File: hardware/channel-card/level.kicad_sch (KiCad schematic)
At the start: 59 parts, among them SW201 MUTE (latching), SW202 DUCK (latching), U201 SSI2162, U202 NE5532, U203 NE5532, U204 TL072, U205 TL072, U206 DG413DY

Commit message: Redraw level sheet with real wires
Pilot for readable sheets: schlayout.py places symbols and draws wires
from KiCad pin geometry, level_wired.py lays out the Level sheet by
circuit block, post_wired.py adds junctions, ground nets, no-connects
and readable field placement. level_build.py stays the reference
netlist. SSI2162 symbol pins rearranged for drawing.

Co-Authored-By: Claude Opus 5.5 <noreply@anthropic.com>
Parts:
- U201: SupplierPN (none) -> 41019302
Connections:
- net +15V: now also R206.1; no longer R206.2
- net AGND: now also C222.1, R220.1, R222.1; no longer C222.2, R220.2, R222.2
- net DUCK_CTRL: now also R222.2; no longer R222.1
- net MUTE_CTRL: now also R220.2; no longer R220.1
- net DUCK_LED: no longer names the net of D204.2 (A), R221.2
- net DUCK_LEDK: no longer names the net of D204.1 (K), SW202.4 (A)
- net DUCK_V: no longer names the net of R217.1, U206.2
- net FADW: no longer names the net of RV201.2, U204.3 (+)
- net L_IIN: no longer names the net of R201.2, U201.2 (IIN1)
- net L_IIN: now also R202.2; no longer R202.1
- net L_INV: no longer names the net of R204.2, R205.1, U203.2 (-)
- net L_IOUT: no longer names the net of C223.1, R203.1, U201.4 (IOUT1), U202.2 (-)
- removed net L_RC: C222.1, R202.2
- net L_VIN: no longer names the net of C221.2, R201.1
- net L_VO: no longer names the net of C223.2, R203.2, R204.1, U202.1
- net MODE: no longer names the net of U201.1 (MODE)
- net MODE: now also R206.2; no longer R206.1
- net MUTE_LED: no longer names the net of D203.2 (A), R219.2
- net MUTE_LEDK: no longer names the net of D203.1 (K), SW201.4 (A)
- net R_IIN: no longer names the net of R251.2, R252.1, U201.9 (IIN2)
- net R_INV: no longer names the net of R254.2, R255.1, U203.6 (-)
- net R_IOUT: no longer names the net of C273.1, R253.1, U201.7 (IOUT2), U202.6 (-)
- net R_RC: no longer names the net of C272.1, R252.2
- net R_VIN: no longer names the net of C271.2, R251.1
- net R_VO: no longer names the net of C273.2, R253.2, R254.1, U202.7
- net SD1IN: no longer names the net of R209.2, R210.2, U204.5 (+)
- net SD1K: no longer names the net of D201.2 (A), R211.1, U204.6 (-)
- net SD1O: no longer names the net of D201.1 (K), U204.7
- net SD2IN: no longer names the net of R212.2, R213.2, U205.3 (+)
- net SD2K: no longer names the net of D202.2 (A), R214.1, U205.2 (-)
- net SD2O: no longer names the net of D202.1 (K), U205.1
- net VB: no longer names the net of R207.1, R209.1, R212.1, U204.1, U204.2 (-)
- net VSUM: no longer names the net of C224.1, R207.2, R208.2, R211.2, R214.2, R215.1, R216.2, U205.6 (-)
- new net: C222.2, R202.1

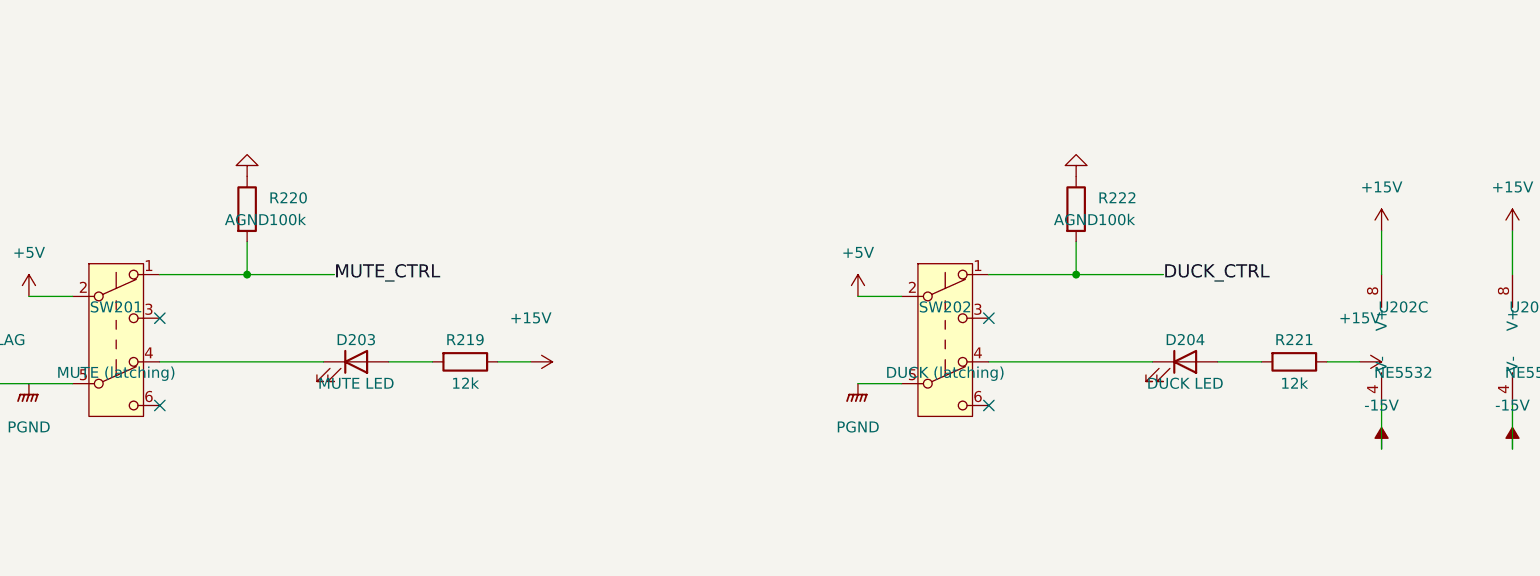
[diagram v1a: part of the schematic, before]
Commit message: Choose GPBS850N latching buttons with printed light caps
Buttons are CW Industries GPBS850N latching DPDT switches (Electrokit)
with 0805 LEDs lighting 3D-printed translucent caps (decision 75).
The datasheet shows pins 2-3 and 5-6 close when pressed, so every
button now uses pin 3 for logic and pin 6 for the LED. Adds the switch
footprint library, rebuild_all.sh, the state-retention requirement for
the momentary-button backlog item, and ten switches to the second
Electrokit order.

Co-Authored-By: Claude Opus 5.5 <noreply@anthropic.com>
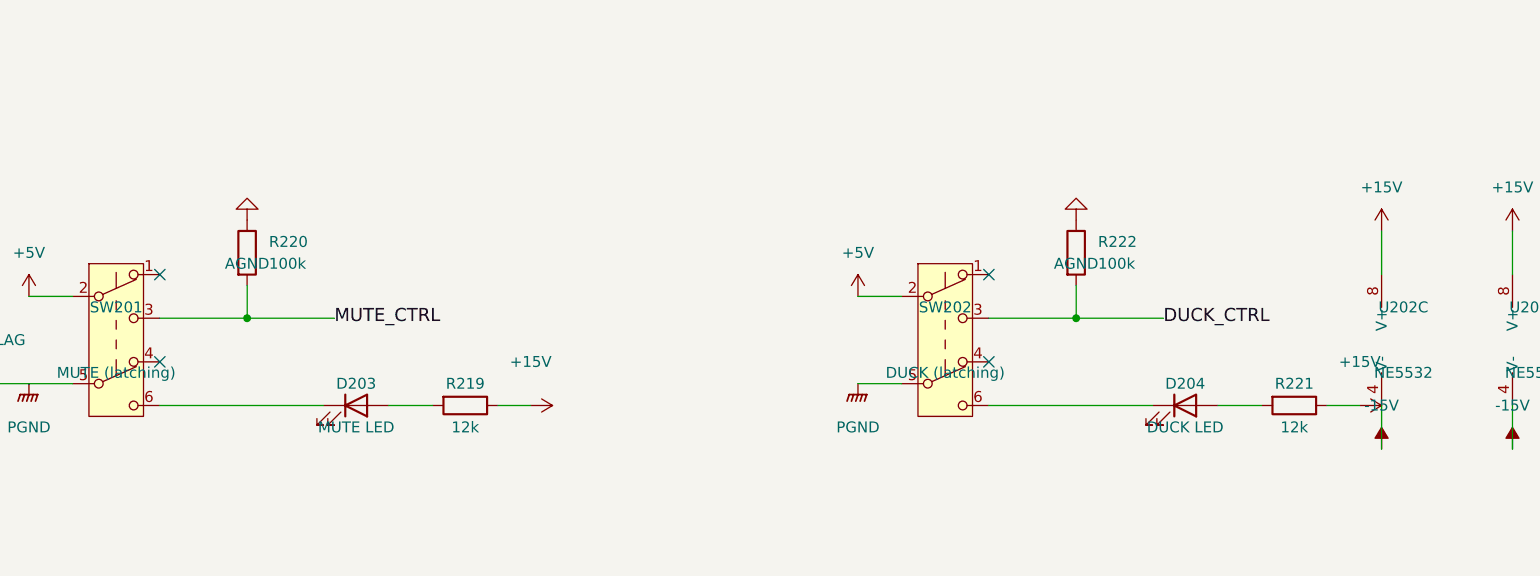
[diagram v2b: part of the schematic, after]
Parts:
- D203, D204: footprint LED_THT:LED_D3.0mm -> LED_SMD:LED_0805_2012Metric
- SW201, SW202: footprint (none) -> syntsamix:SW_Latching_8.5x8.5mm_CW_GPBS850N; MPN (none) -> GPBS850N; Manufacturer (none) -> CW Industries; Supplier (none) -> Electrokit; SupplierPN (none) -> 41012905
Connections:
- net DUCK_CTRL: now also SW202.3 (C); no longer SW202.1 (A)
- net MUTE_CTRL: now also SW201.3 (C); no longer SW201.1 (A)
- net at D203.1 (K): now also SW201.6 (C); no longer SW201.4 (A)
- net at D204.1 (K): now also SW202.6 (C); no longer SW202.4 (A)

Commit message: Add test pads to the channel card sheets
24 bare 1.5 mm test pads on key audio, control and ground nets across
the Input, Filter, Level, Routing and Meter sheets, named by net and
kept out of the BOM (decision 77). Each pad is in the reference
netlists, so the checks prove it sits on the intended net.

Co-Authored-By: Claude Opus 5.5 <noreply@anthropic.com>
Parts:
- added TP201: VC, TestPoint:TestPoint_Pad_D1.5mm, symbol Connector:TestPoint
- added TP202: VB, TestPoint:TestPoint_Pad_D1.5mm, symbol Connector:TestPoint
- added TP203: L_POSTFADE, TestPoint:TestPoint_Pad_D1.5mm, symbol Connector:TestPoint
- added TP204: R_POSTFADE, TestPoint:TestPoint_Pad_D1.5mm, symbol Connector:TestPoint
- added TP205: SC_ENV, TestPoint:TestPoint_Pad_D1.5mm, symbol Connector:TestPoint
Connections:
- net L_POSTFADE: now also TP203.1
- net R_POSTFADE: now also TP204.1
- net SC_ENV: now also TP205.1
- net VC: now also TP201.1
- net at R207.1, R209.1, R212.1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: now also TP202.1

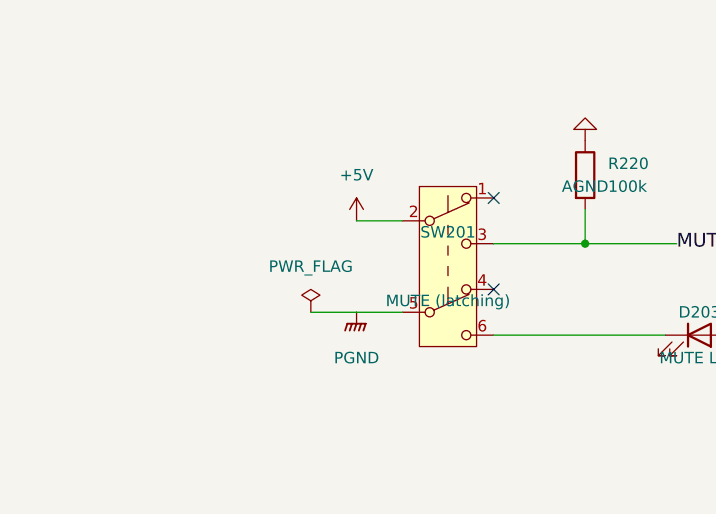
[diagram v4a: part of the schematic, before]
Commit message: Add chain and power sheet; channel card schematic complete
Audio and power ribbon IN/OUT headers wired straight through,
LM317/LM337 regulators to +/-15.2 V with ADJ bypass and protection
diodes, SS14 rail clamps, 78L05 for +5 V, and test pads for the rails
(decision 78). Power flags moved to this sheet. The whole channel card
now passes ERC with 0 errors and 0 warnings and every sheet matches its
reference netlist. Records the open power-ribbon current question in
CHAIN.md.

Co-Authored-By: Claude Opus 5.5 <noreply@anthropic.com>
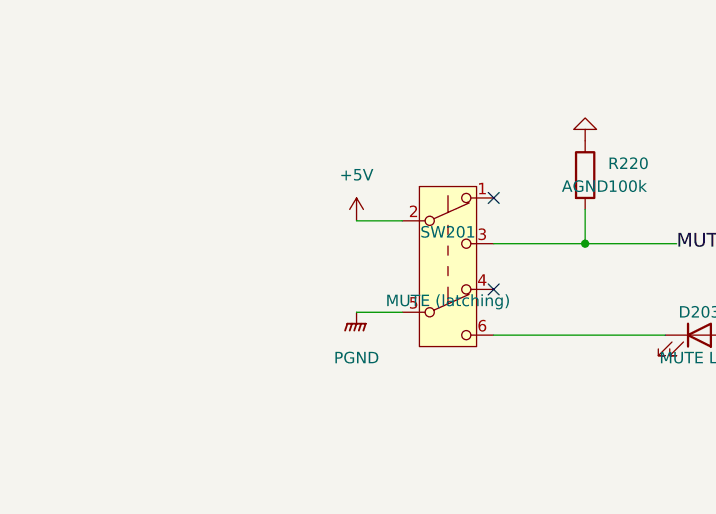
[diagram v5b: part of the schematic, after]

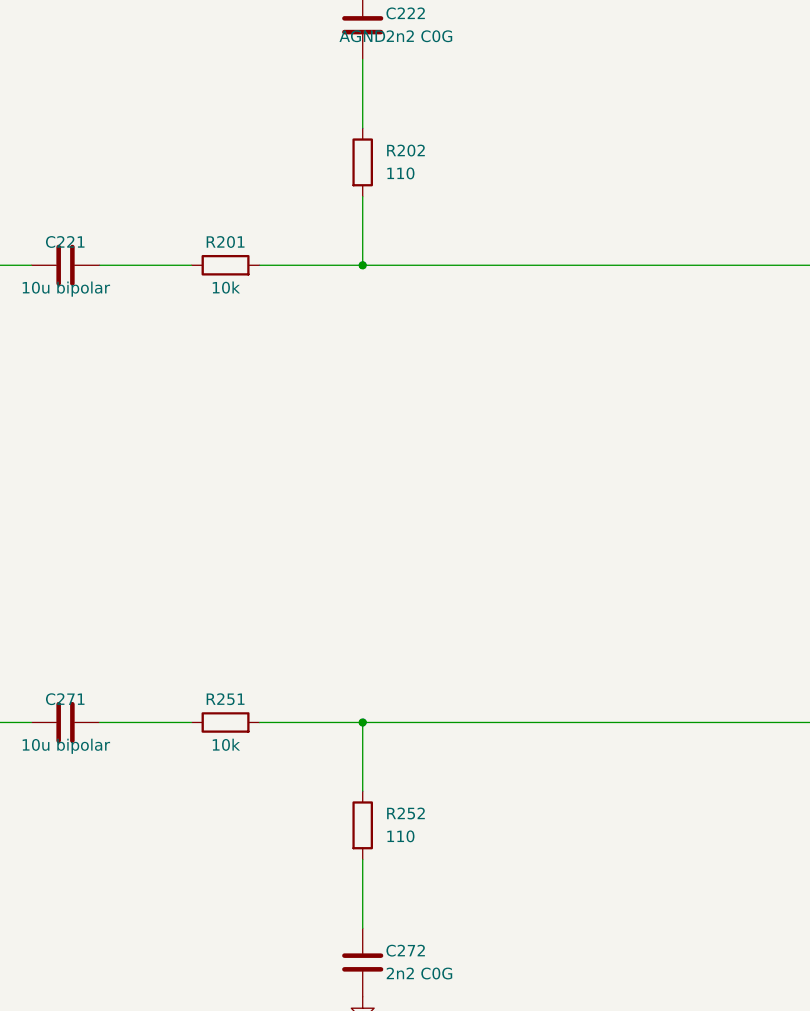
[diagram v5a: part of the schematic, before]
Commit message: Check parts against LCSC stock and use basic resistor values
tools/lcsc_check.py checks docs/parts.csv against the JLCPCB/LCSC
catalogue and writes docs/lcsc-check.csv. Non-critical resistors move
to JLC basic values to cut setup fees (decision 79): bus resistors 22k,
VCA input network 100R, cutoff offset 470k, regulator dividers 200R/2k2
(15.1 V). All sheets rebuilt and verified (ERC 0/0).

Co-Authored-By: Claude Opus 5.5 <noreply@anthropic.com>
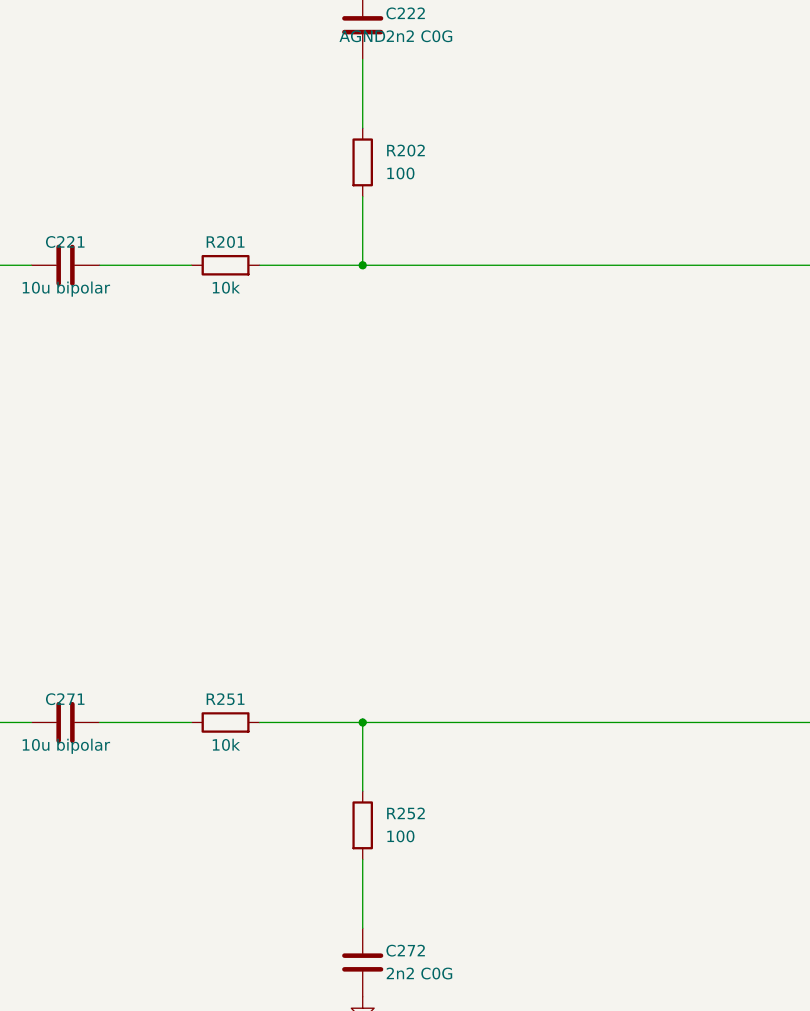
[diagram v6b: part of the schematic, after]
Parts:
- R202, R252: value 110 -> 100; ProjectPN SX-R-022 -> SX-R-001

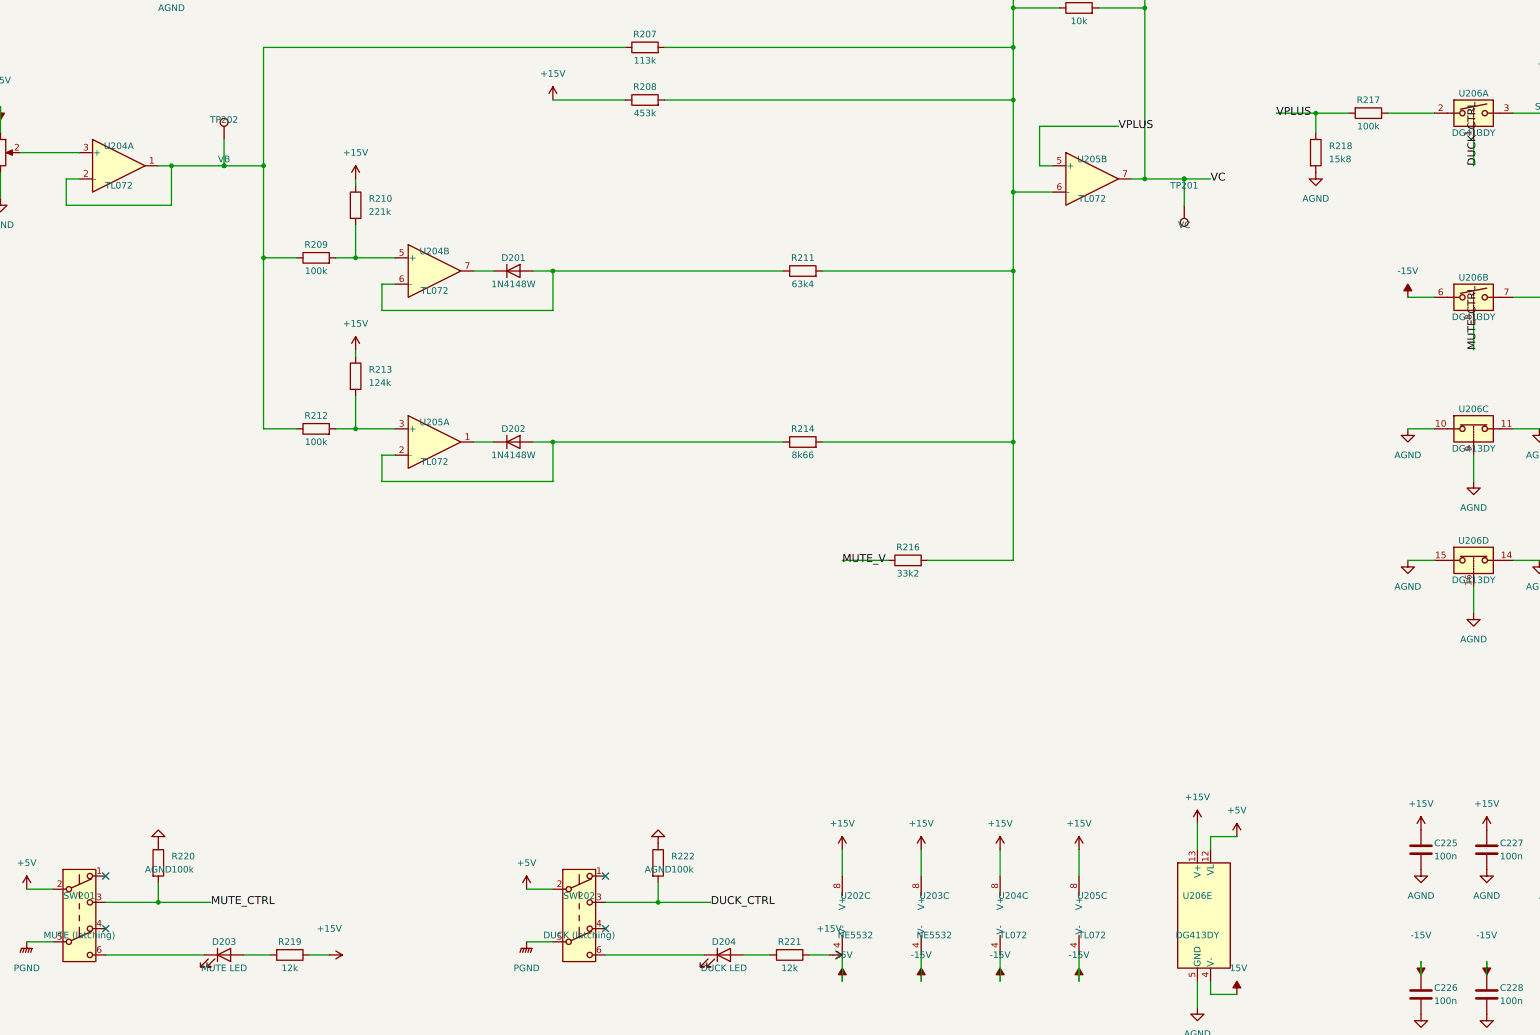
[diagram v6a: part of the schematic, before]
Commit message: Channel card: draw decisions 97 and 98, fader buffer on an OPA2171 (decision 102)
- Level: SC_ENV into the summer's virtual earth through R217 30k1, R218 removed,
  summer + input on AGND (decision 97)
- Q301 emitter and button pull-downs R17, R186, R220, R222, R313, R315, R317 to PGND (decision 98)
- U204 = OPA2171 for the fader buffer and control summer (input range includes V-);
  superdiodes moved to the TL072 U205 (decision 102)
- simulation/level: fader law within 1.2 dB, ducking 10.07 dB per -1 V at every fader position
- Power budget, parts list, STATUS, breadboard test 10 and working notes updated

Co-Authored-By: Claude Opus 5.5 <noreply@anthropic.com>
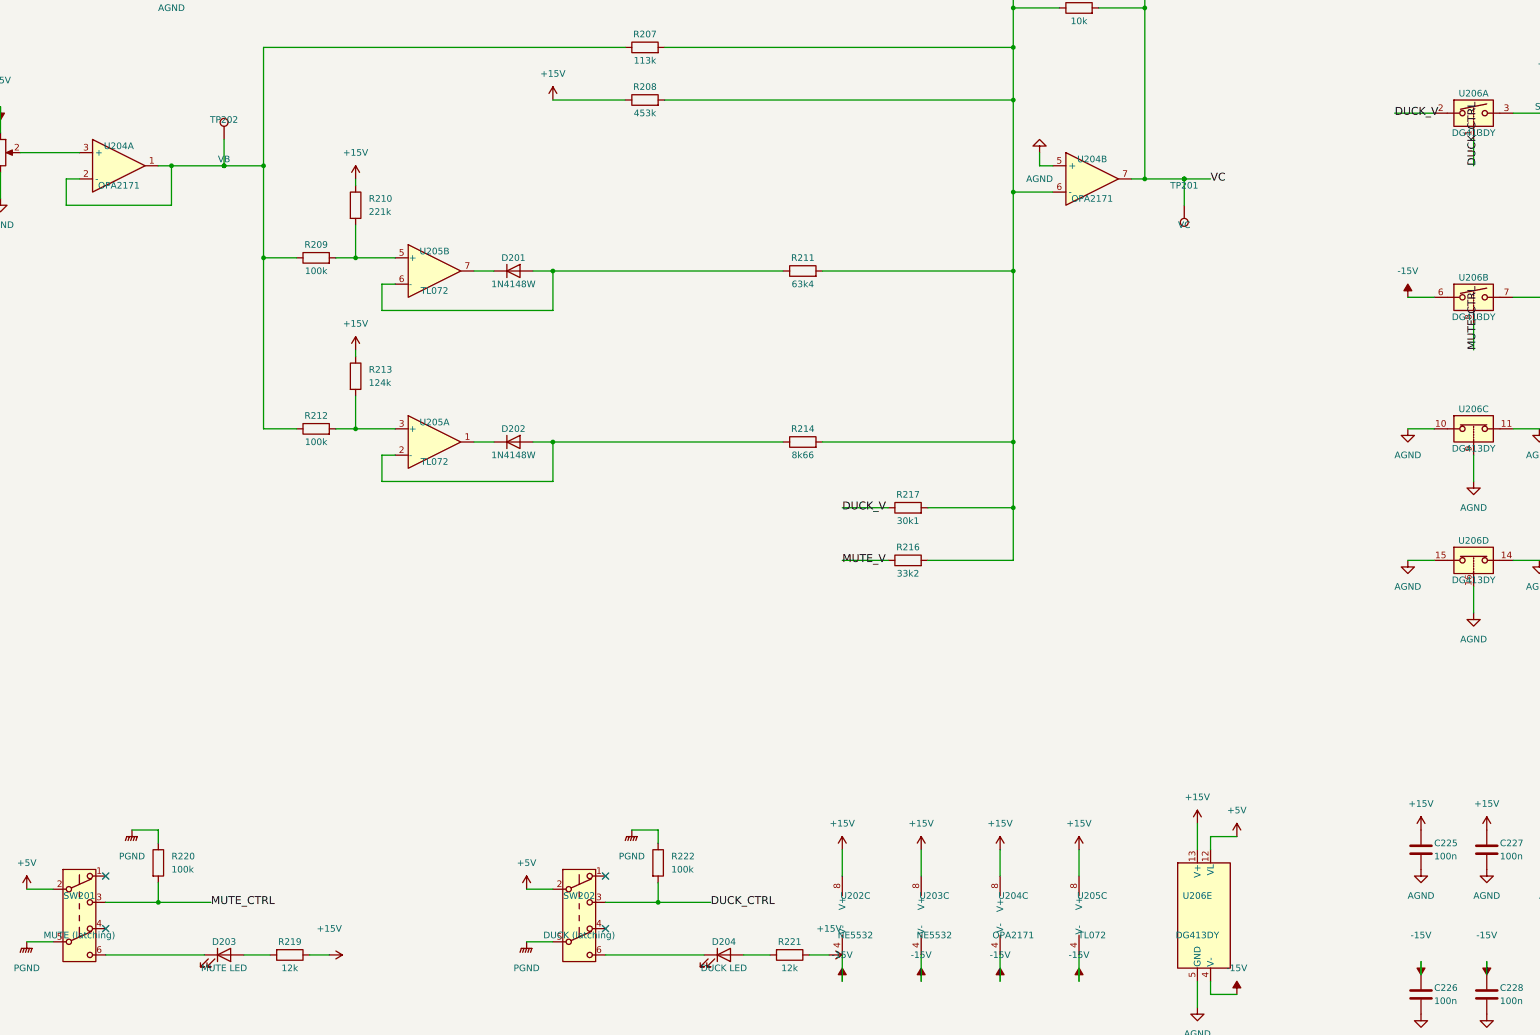
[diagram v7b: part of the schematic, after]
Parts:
- removed R218: 15k8, Resistor_SMD:R_0805_2012Metric, symbol Device:R
- removed U204: TL072, Package_SO:SOIC-8_3.9x4.9mm_P1.27mm, symbol Amplifier_Operational:TL072
- added U204: OPA2171, Package_SO:SOIC-8_3.9x4.9mm_P1.27mm, symbol Amplifier_Operational:Opamp_Dual
- R217: value 100k -> 30k1; Note (none) -> SC_ENV into the virtual earth: 0.332 V/V, 10 dB of ducking 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; ProjectPN SX-R-007 -> SX-R-087
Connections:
- net +15V: now also U204.8 (V+)
- net -15V: now also U204.4 (V-)
- net AGND: now also U204.5 (+); no longer R220.1, R222.1
- net PGND: now also R220.1, R222.1
- net VC: now also U204.7; no longer U205.7
- net at R207.1, R209.1, R212.1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: now also U204.1, U204.2 (-)
- net at C224.1, R207.2, R208.2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: now also R217.2, U204.6 (-); no longer U205.6 (-)
- net DUCK_V: now reaches R217.1, U206.2
- net at RV201.2: now also U204.3 (+)
- net at D201.2 (A), R211.1: now also U205.6 (-)
- net at D201.1 (K): now also U205.7
- net at R209.2, R210.2: now also U205.5 (+)
- removed net VPLUS: R217.2, U205.5 (+)
